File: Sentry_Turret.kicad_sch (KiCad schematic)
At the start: 36 parts, among them J14 501645-1620, J16 172298-1108

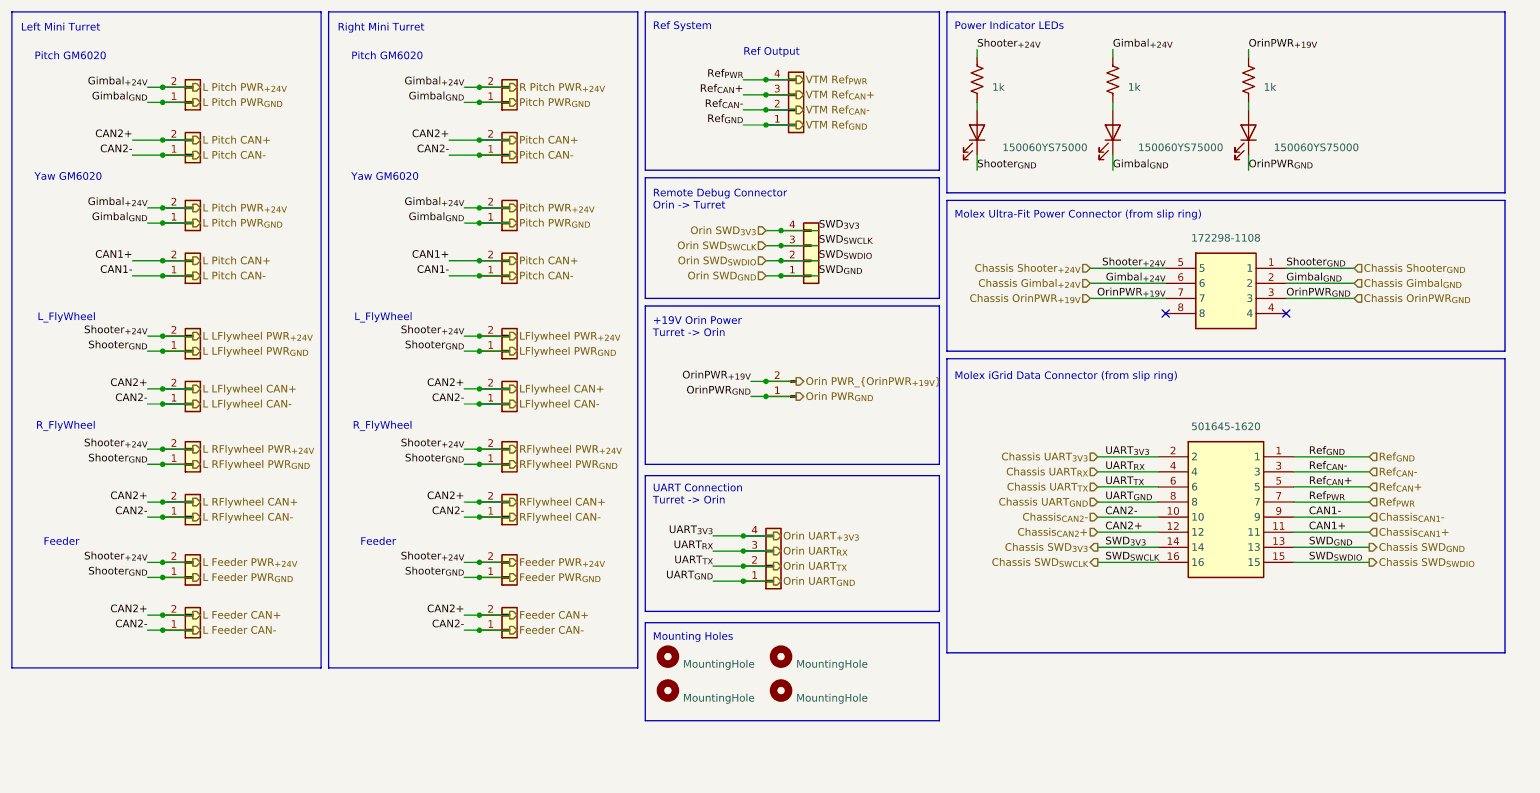
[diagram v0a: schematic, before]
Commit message: Finalized schematic, began layout
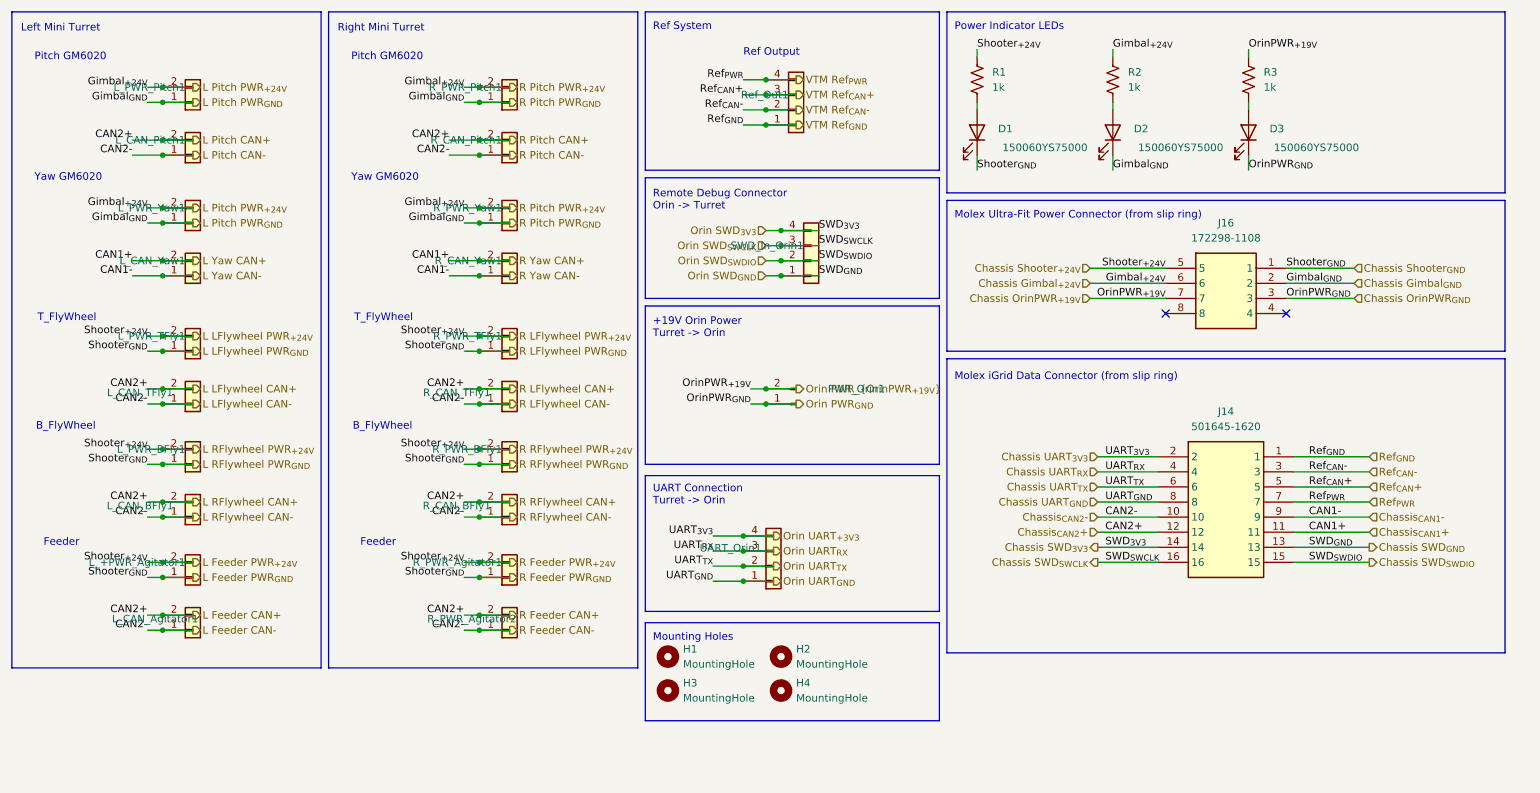
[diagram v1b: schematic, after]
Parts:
- H1, H2, H3, H4: footprint MountingHole:MountingHole_3mm -> MountingHole:MountingHole_3.2mm_M3
- renumbered L_+PWR_Agitator to L_+PWR_Agitator1, L_CAN_Agitator to L_CAN_Agitator1, L_CAN_RFly to L_CAN_BFly1, L_CAN_Pitch to L_CAN_Pitch1, L_CAN_LFly to L_CAN_TFly1, L_CAN_Yaw to L_CAN_Yaw1, L_PWR_RFly to L_PWR_BFly1, L_PWR_Pitch to L_PWR_Pitch1, L_PWR_LFly to L_PWR_TFly1, L_PWR_Yaw to L_PWR_Yaw1, PWR_Orin to PWR_Orin1, R_CAN_RFly to R_CAN_BFly1, R_CAN_Pitch to R_CAN_Pitch1, R_CAN_LFly to R_CAN_TFly1, R_CAN_Yaw to R_CAN_Yaw1, R_PWR_Agitator to R_PWR_Agitator1, R_PWR_Agitator to R_PWR_Agitator2, R_PWR_RFly to R_PWR_BFly1, R_PWR_Pitch to R_PWR_Pitch1, R_PWR_LFly to R_PWR_TFly1, R_PWR_Yaw to R_PWR_Yaw1, SWD_In_Orin to SWD_In_Orin1, UART_Orin to UART_Orin1
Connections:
- net Chassis_{CAN1}+: no longer J14.12, L_CAN_Agitator1.2 (Pin_2), L_CAN_BFly1.2 (Pin_2), L_CAN_Pitch1.2 (Pin_2), L_CAN_TFly1.2 (Pin_2), R_CAN_BFly1.2 (Pin_2), R_CAN_Pitch1.2 (Pin_2), R_CAN_TFly1.2 (Pin_2), R_PWR_Agitator2.2 (Pin_2)
- net Chassis_{CAN1}-: no longer J14.10, L_CAN_Agitator1.1 (Pin_1), L_CAN_BFly1.1 (Pin_1), L_CAN_Pitch1.1 (Pin_1), L_CAN_TFly1.1 (Pin_1), R_CAN_BFly1.1 (Pin_1), R_CAN_Pitch1.1 (Pin_1), R_CAN_TFly1.1 (Pin_1), R_PWR_Agitator2.1 (Pin_1)
- new net Chassis_{CAN2}+: J14.12, L_CAN_Agitator1.2 (Pin_2), L_CAN_BFly1.2 (Pin_2), L_CAN_Pitch1.2 (Pin_2), L_CAN_TFly1.2 (Pin_2), R_CAN_BFly1.2 (Pin_2), R_CAN_Pitch1.2 (Pin_2), R_CAN_TFly1.2 (Pin_2), R_PWR_Agitator2.2 (Pin_2)
- new net Chassis_{CAN2}-: J14.10, L_CAN_Agitator1.1 (Pin_1), L_CAN_BFly1.1 (Pin_1), L_CAN_Pitch1.1 (Pin_1), L_CAN_TFly1.1 (Pin_1), R_CAN_BFly1.1 (Pin_1), R_CAN_Pitch1.1 (Pin_1), R_CAN_TFly1.1 (Pin_1), R_PWR_Agitator2.1 (Pin_1)
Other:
- note added: "B_FlyWheel"
- note added: "T_FlyWheel"
- note removed: "L_FlyWheel"
- note removed: "R_FlyWheel"

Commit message: Check for jed
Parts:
- added L_Light1, R_Light1: Conn_01x02_Pin, Connector_AMASS:AMASS_XT30U-F_1x02_P5.0mm_Vertical, symbol Connector_Generic:Conn_01x02
- renumbered L_+PWR_Agitator1 to L_PWR_Agitator1
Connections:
- net Chassis Shooter_{+24V}: now also L_Light1.2 (Pin_2), R_Light1.2 (Pin_2)
- net Chassis Shooter_{GND}: now also L_Light1.1 (Pin_1), R_Light1.1 (Pin_1)
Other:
- note added: "Bottom FlyWheel"
- note added: "Top FlyWheel"
- note added: "UV Light Module"
- note removed: "B_FlyWheel"
- note removed: "T_FlyWheel"

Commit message: Layout review
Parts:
- added Ref_Out2: Conn_01x04_Pin, Connector_JST:JST_GH_BM04B-GHS-TBT_1x04-1MP_P1.25mm_Vertical, symbol Connector_Generic:Conn_01x04
- added TP1, TP2, TP3: TestPoint, TestPoint:TestPoint_2Pads_Pitch2.54mm_Drill0.8mm, symbol Connector:TestPoint
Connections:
- net Chassis Gimbal_{+24V}: now also TP2.1
- net Chassis OrinPWR_{+19V}: now also J16.8, TP3.1; no longer J16.7
- net Chassis OrinPWR_{GND}: now also J16.4; no longer J16.3
- net Chassis Shooter_{+24V}: now also J16.7, TP1.1; no longer J16.5
- net Chassis Shooter_{GND}: now also J16.3; no longer J16.1
- net Ref_{CAN}+: now also Ref_Out2.3 (Pin_3)
- net Ref_{CAN}-: now also Ref_Out2.2 (Pin_2)
- net Ref_{GND}: now also Ref_Out2.1 (Pin_1)
- net Ref_{PWR}: now also Ref_Out2.4 (Pin_4)
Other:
- note added: "Ref Output 1"
- note added: "Ref Output 2"
- note removed: "Ref Output"

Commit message: Finalized board for order
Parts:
- removed TP1, TP2, TP3: TestPoint, TestPoint:TestPoint_2Pads_Pitch2.54mm_Drill0.8mm, symbol Connector:TestPoint
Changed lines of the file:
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@@
 	)
 	(junction
-		(at 223.52 22.86)
-		(diameter 0)
-		(color 0 0 0 0)
-	)
-	(junction
 		(at 93.98 57.15)
 		(diameter 0)
@@
 	)
 	(junction
-		(at 200.66 22.86)
-		(diameter 0)
-		(color 0 0 0 0)
-	)
-	(junction
 		(at 140.97 30.48)
 		(diameter 0)
@@
 	)
 	(junction
-		(at 177.8 22.86)
-		(diameter 0)
-		(color 0 0 0 0)
-	)
-	(junction
 		(at 144.78 64.77)
 		(diameter 0)
@@
 		(length 2.54)
 		(shape round)
+		(at 138.43 48.26 180)
+		(fields_autoplaced yes)
+		(effects
+			(font
+				(size 1.27 1.27)
+			)
+			(justify right bottom)
+		)
+		(property "Netclass" "Power"
+			(at 139.1285 50.8 0)
+			(effects
+				(font
+					(size 1.27 1.27)
+				)
+				(justify left)
+			)
+		)
+		(property "Component Class" ""
+			(at -44.45 31.75 0)
+			(effects
+				(font
+					(size 1.27 1.27)
+					(italic yes)
+				)
+				(justify right)
+			)
+		)
+	)
+	(netclass_flag ""
+		(length 2.54)
+		(shape round)
+		(at 138.43 40.64 0)
+		(fields_autoplaced yes)
+		(effects
+			(font
+				(size 1.27 1.27)
+			)
+			(justify left bottom)
+		)
+		(property "Netclass" "Power"
+			(at 139.1285 38.1 0)
+			(effects
+				(font
+					(size 1.27 1.27)
+				)
+				(justify left)
+			)
+		)
+		(property "Component Class" ""
+			(at -44.45 24.13 0)
+			(effects
+				(font
+					(size 1.27 1.27)
+					(italic yes)
+				)
+			)
+		)
+	)
+	(netclass_flag ""
+		(length 2.54)
+		(shape round)
 		(at 138.43 33.02 180)
 		(fields_autoplaced yes)
@@
 	)
 	(symbol
-		(lib_id "Connector:TestPoint")
-		(at 200.66 22.86 270)
-		(unit 1)
-		(exclude_from_sim no)
-		(in_bom yes)
-		(on_board yes)
-		(dnp no)
-		(fields_autoplaced yes)
-		(property "Reference" "TP2"
-			(at 205.74 21.5899 90)
-			(effects
-				(font
-					(size 1.27 1.27)
-				)
-				(justify left)
-			)
-		)
-		(property "Value" "TestPoint"
-			(at 205.74 24.1299 90)
-			(effects
-				(font
-					(size 1.27 1.27)
-				)
-				(justify left)
-			)
-		)
-		(property "Footprint" "TestPoint:TestPoint_2Pads_Pitch2.54mm_Drill0.8mm"
-			(at 200.66 27.94 0)
-			(effects
-				(font
-					(size 1.27 1.27)
-				)
-				(hide yes)
-			)
-		)
-		(property "Datasheet" "~"
-			(at 200.66 27.94 0)
-			(effects
-				(font
-					(size 1.27 1.27)
-				)
-				(hide yes)
-			)
-		)
-		(property "Description" "test point"
-			(at 200.66 22.86 0)
-			(effects
-				(font
-					(size 1.27 1.27)
-				)
-				(hide yes)
-			)
-		)
-		(pin "1"
-		)
-		(instances
-			(project "Sentry_Turret"
-				(path "/1af64243-237e-4d0e-bea9-8a84ac1ea3bc"
-					(reference "TP2")
-					(unit 1)
-				)
-			)
-		)
-	)
-	(symbol
 		(lib_id "Connector_Generic:Conn_01x02")
 		(at 45.72 50.8 0)
@@
 	)
 	(symbol
-		(lib_id "Connector:TestPoint")
-		(at 177.8 22.86 270)
-		(unit 1)
-		(exclude_from_sim no)
-		(in_bom yes)
-		(on_board yes)
-		(dnp no)
-		(fields_autoplaced yes)
-		(property "Reference" "TP1"
-			(at 182.88 21.5899 90)
-			(effects
-				(font
-					(size 1.27 1.27)
-				)
-				(justify left)
-			)
-		)
-		(property "Value" "TestPoint"
-			(at 182.88 24.1299 90)
-			(effects
-				(font
-					(size 1.27 1.27)
-				)
-				(justify left)
-			)
-		)
-		(property "Footprint" "TestPoint:TestPoint_2Pads_Pitch2.54mm_Drill0.8mm"
-			(at 177.8 27.94 0)
-			(effects
-				(font
-					(size 1.27 1.27)
-				)
-				(hide yes)
-			)
-		)
-		(property "Datasheet" "~"
-			(at 177.8 27.94 0)
-			(effects
-				(font
-					(size 1.27 1.27)
-				)
-				(hide yes)
-			)
-		)
-		(property "Description" "test point"
-			(at 177.8 22.86 0)
-			(effects
-				(font
-					(size 1.27 1.27)
-				)
-				(hide yes)
-			)
-		)
-		(pin "1"
-		)
-		(instances
-			(project ""
-				(path "/1af64243-237e-4d0e-bea9-8a84ac1ea3bc"
-					(reference "TP1")
-					(unit 1)
-				)
-			)
-		)
-	)
-	(symbol
 		(lib_id "Mechanical:MountingHole")
 		(at 144.78 139.7 0)
@@
 					(unit 1)
 				)
-			)
-		)
-	)
-	(symbol
-		(lib_id "Connector:TestPoint")
-		(at 223.52 22.86 270)
-		(unit 1)
-		(exclude_from_sim no)
-		(in_bom yes)
-		(on_board yes)
-		(dnp no)
-		(fields_autoplaced yes)
-		(property "Reference" "TP3"
-			(at 228.6 21.5899 90)
-			(effects
-				(font
-					(size 1.27 1.27)
-				)
-				(justify left)
-			)
-		)
-		(property "Value" "TestPoint"
-			(at 228.6 24.1299 90)
-			(effects
-				(font
-					(size 1.27 1.27)
-				)
-				(justify left)
-			)
-		)
-		(property "Footprint" "TestPoint:TestPoint_2Pads_Pitch2.54mm_Drill0.8mm"
-			(at 223.52 27.94 0)
-			(effects
-				(font
-					(size 1.27 1.27)
-				)
-				(hide yes)
-			)
-		)
-		(property "Datasheet" "~"
-			(at 223.52 27.94 0)
-			(effects
-				(font
-					(size 1.27 1.27)
-				)
-				(hide yes)
-			)
-		)
-		(property "Description" "test point"
-			(at 223.52 22.86 0)
-			(effects
-				(font
-					(size 1.27 1.27)
-				)
-				(hide yes)
-			)
-		)
-		(pin "1"
-		)
-		(instances
-			(project "Sentry_Turret"
-				(path "/1af64243-237e-4d0e-bea9-8a84ac1ea3bc"
-					(reference "TP3")
-					(unit 1)
-				)
